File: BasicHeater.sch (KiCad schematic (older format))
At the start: 10 parts, among them J13 Thermistor

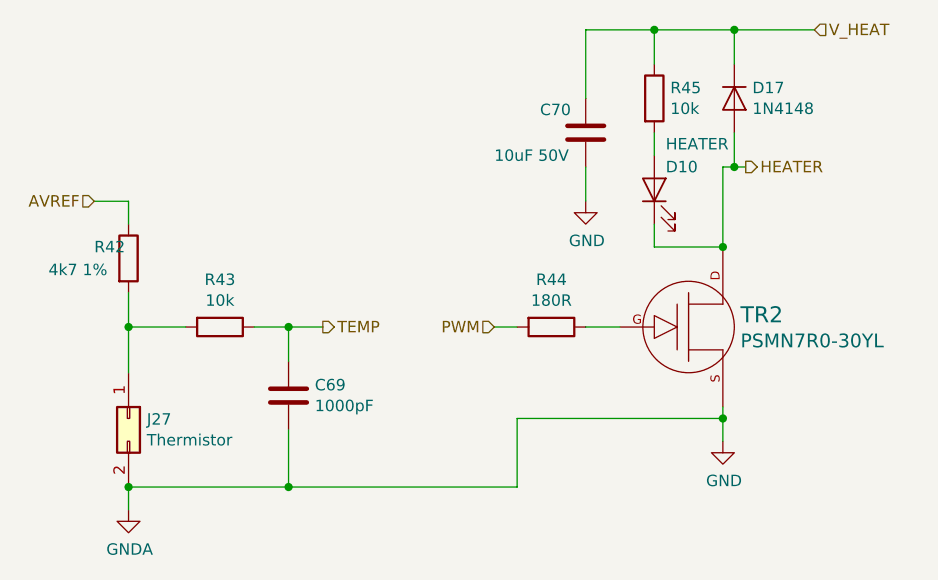
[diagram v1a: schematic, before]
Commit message: Add missing files from the TMC2130 branch.
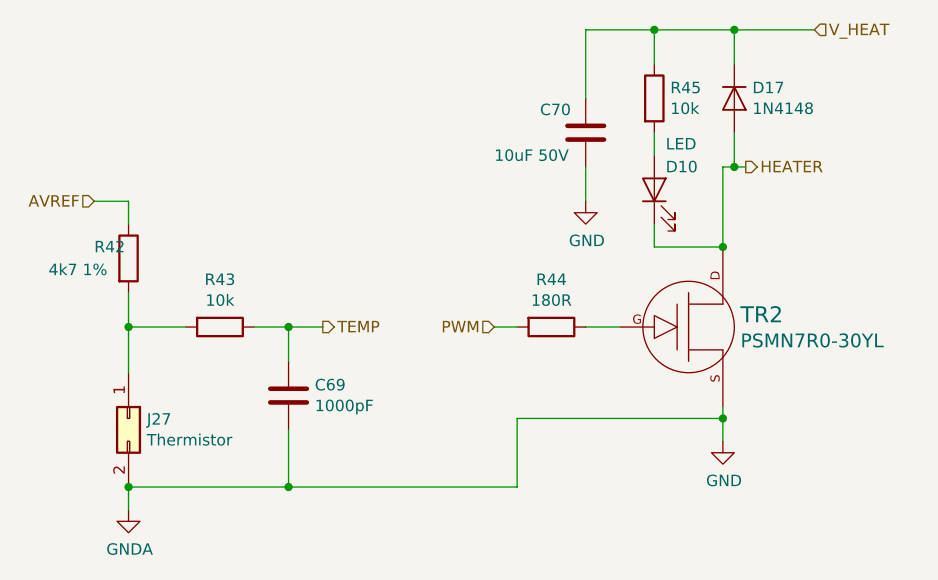
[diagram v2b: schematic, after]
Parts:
- C16: footprint Capacitor_SMD:C_0603_1608Metric -> PrntrBoardV1:C_0603_1608Metric
- C17: footprint Capacitor_SMD:C_1206_3216Metric -> PrntrBoardV1:C_1206_3216Metric
- D2: value HEATER -> LED
- R10, R11, R8, R9: footprint Resistor_SMD:R_0603_1608Metric -> PrntrBoardV1:R_0603_1608Metric
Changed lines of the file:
@@
 F 0 "R42" H 2800 3000 50  0000 L CNN
 F 1 "4k7 1%" H 2600 2900 50  0000 L CNN
-F 2 "Resistor_SMD:R_0603_1608Metric" V 2880 2950 50  0001 C CNN
+F 2 "PrntrBoardV1:R_0603_1608Metric" V 2880 2950 50  0001 C CNN
 F 3 "~" H 2950 2950 50  0001 C CNN
 	1    2950 2950
@@
 F 0 "R43" V 3143 3250 50  0000 C CNN
 F 1 "10k" V 3234 3250 50  0000 C CNN
-F 2 "Resistor_SMD:R_0603_1608Metric" V 3280 3250 50  0001 C CNN
+F 2 "PrntrBoardV1:R_0603_1608Metric" V 3280 3250 50  0001 C CNN
 F 3 "~" H 3350 3250 50  0001 C CNN
 	1    3350 3250
@@
 F 0 "C69" H 3765 3596 50  0000 L CNN
 F 1 "1000pF" H 3765 3505 50  0000 L CNN
-F 2 "Capacitor_SMD:C_0603_1608Metric" H 3688 3400 50  0001 C CNN
+F 2 "PrntrBoardV1:C_0603_1608Metric" H 3688 3400 50  0001 C CNN
 F 3 "~" H 3650 3550 50  0001 C CNN
 	1    3650 3550
@@
 F 0 "R44" V 4593 3250 50  0000 C CNN
 F 1 "180R" V 4684 3250 50  0000 C CNN
-F 2 "Resistor_SMD:R_0603_1608Metric" V 4730 3250 50  0001 C CNN
+F 2 "PrntrBoardV1:R_0603_1608Metric" V 4730 3250 50  0001 C CNN
 F 3 "~" H 4800 3250 50  0001 C CNN
 	1    4800 3250
@@
 F 0 "C70" H 4750 2500 50  0000 L CNN
 F 1 "10uF 50V" H 4550 2300 50  0000 L CNN
-F 2 "Capacitor_SMD:C_1206_3216Metric" H 4950 2400 50  0001 C CNN
+F 2 "PrntrBoardV1:C_1206_3216Metric" H 4950 2400 50  0001 C CNN
 F 3 "~" H 4950 2400 50  0001 C CNN
 	1    4950 2400
@@
 F 0 "R45" H 5320 2296 50  0000 L CNN
 F 1 "10k" H 5320 2205 50  0000 L CNN
-F 2 "Resistor_SMD:R_0603_1608Metric" V 5180 2250 50  0001 C CNN
+F 2 "PrntrBoardV1:R_0603_1608Metric" V 5180 2250 50  0001 C CNN
 F 3 "~" H 5250 2250 50  0001 C CNN
 	1    5250 2250
@@
 AR Path="/5AB8F10D/5ACEEAB5" Ref="D11"  Part="1"
 F 0 "D10" V 5350 2600 50  0000 R CNN
-F 1 "HEATER" V 5450 2600 50  0000 R CNN
+F 1 "LED" V 5450 2600 50  0000 R CNN
 F 2 "PrntrBoardV1:LED_0603_1608Metric" H 5250 2650 50  0001 C CNN
 F 3 "~" H 5250 2650 50  0001 C CNN

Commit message: Reset schematics for tmc2660. Clean the board layout.
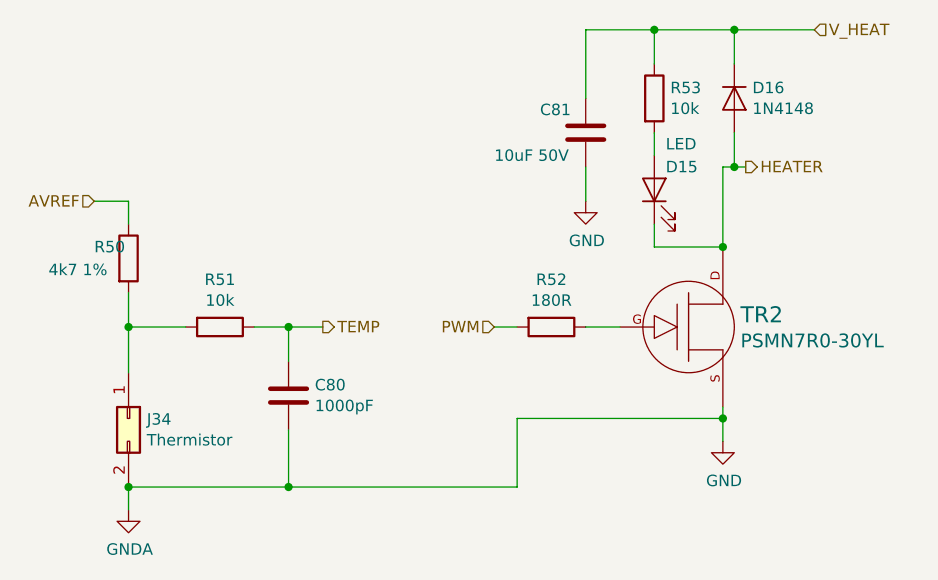
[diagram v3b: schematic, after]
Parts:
- renumbered C16 to C23, C17 to C24, D17 to D16, D2 to D6, J13 to J20, R8 to R16, R9 to R17, R10 to R18, R11 to R19
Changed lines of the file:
@@
 $EndDescr
 $Comp
-L Connector_Generic:Conn_02x01 J13
+L Connector_Generic:Conn_02x01 J20
 U 1 1 5ACEEAAB
 P 2950 3650
-AR Path="/5AC337B6/5ACBE919/5AD4D269/5ACEEAAB" Ref="J13"  Part="1"
-AR Path="/5AC337B6/5AD9F95A/5AD4D269/5ACEEAAB" Ref="J27"  Part="1"
-AR Path="/5AB8F10D/5ACEEAAB" Ref="J28"  Part="1"
-F 0 "J27" V 2954 3730 50  0000 L CNN
+AR Path="/5AC337B6/5ACBE919/5AD4D269/5ACEEAAB" Ref="J20"  Part="1"
+AR Path="/5AC337B6/5AD9F95A/5AD4D269/5ACEEAAB" Ref="J34"  Part="1"
+AR Path="/5AB8F10D/5ACEEAAB" Ref="J?"  Part="1"
+F 0 "J34" V 2954 3730 50  0000 L CNN
 F 1 "Thermistor" V 3045 3730 50  0000 L CNN
 F 2 "Connector_PinHeader_2.54mm:PinHeader_1x02_P2.54mm_Vertical" H 2950 3650 50  0001 C CNN
@@
 $EndComp
 $Comp
-L power:GNDA #PWR020
+L power:GNDA #PWR031
 U 1 1 5ACEEAAC
 P 2950 4050
-AR Path="/5AC337B6/5ACBE919/5AD4D269/5ACEEAAC" Ref="#PWR020"  Part="1"
-AR Path="/5AC337B6/5AD9F95A/5AD4D269/5ACEEAAC" Ref="#PWR065"  Part="1"
-AR Path="/5AB8F10D/5ACEEAAC" Ref="#PWR068"  Part="1"
-F 0 "#PWR065" H 2950 3800 50  0001 C CNN
+AR Path="/5AC337B6/5ACBE919/5AD4D269/5ACEEAAC" Ref="#PWR031"  Part="1"
+AR Path="/5AC337B6/5AD9F95A/5AD4D269/5ACEEAAC" Ref="#PWR076"  Part="1"
+AR Path="/5AB8F10D/5ACEEAAC" Ref="#PWR?"  Part="1"
+F 0 "#PWR076" H 2950 3800 50  0001 C CNN
 F 1 "GNDA" H 2955 3877 50  0000 C CNN
 F 2 "" H 2950 4050 50  0001 C CNN
@@
 $EndComp
 $Comp
-L Device:R R8
+L Device:R R16
 U 1 1 5ACEEAAD
 P 2950 2950
-AR Path="/5AC337B6/5ACBE919/5AD4D269/5ACEEAAD" Ref="R8"  Part="1"
-AR Path="/5AC337B6/5AD9F95A/5AD4D269/5ACEEAAD" Ref="R42"  Part="1"
-AR Path="/5AB8F10D/5ACEEAAD" Ref="R46"  Part="1"
-F 0 "R42" H 2800 3000 50  0000 L CNN
+AR Path="/5AC337B6/5ACBE919/5AD4D269/5ACEEAAD" Ref="R16"  Part="1"
+AR Path="/5AC337B6/5AD9F95A/5AD4D269/5ACEEAAD" Ref="R50"  Part="1"
+AR Path="/5AB8F10D/5ACEEAAD" Ref="R?"  Part="1"
+F 0 "R50" H 2800 3000 50  0000 L CNN
 F 1 "4k7 1%" H 2600 2900 50  0000 L CNN
 F 2 "PrntrBoardV1:R_0603_1608Metric" V 2880 2950 50  0001 C CNN
@@
 $EndComp
 $Comp
-L Device:R R9
+L Device:R R17
 U 1 1 5ACEEAAE
 P 3350 3250
-AR Path="/5AC337B6/5ACBE919/5AD4D269/5ACEEAAE" Ref="R9"  Part="1"
-AR Path="/5AC337B6/5AD9F95A/5AD4D269/5ACEEAAE" Ref="R43"  Part="1"
-AR Path="/5AB8F10D/5ACEEAAE" Ref="R47"  Part="1"
-F 0 "R43" V 3143 3250 50  0000 C CNN
+AR Path="/5AC337B6/5ACBE919/5AD4D269/5ACEEAAE" Ref="R17"  Part="1"
+AR Path="/5AC337B6/5AD9F95A/5AD4D269/5ACEEAAE" Ref="R51"  Part="1"
+AR Path="/5AB8F10D/5ACEEAAE" Ref="R?"  Part="1"
+F 0 "R51" V 3143 3250 50  0000 C CNN
 F 1 "10k" V 3234 3250 50  0000 C CNN
 F 2 "PrntrBoardV1:R_0603_1608Metric" V 3280 3250 50  0001 C CNN
@@
 $EndComp
 $Comp
-L Device:C C16
+L Device:C C23
 U 1 1 5AD4D569
 P 3650 3550
-AR Path="/5AC337B6/5ACBE919/5AD4D269/5AD4D569" Ref="C16"  Part="1"
-AR Path="/5AC337B6/5AD9F95A/5AD4D269/5AD4D569" Ref="C69"  Part="1"
-AR Path="/5AB8F10D/5AD4D569" Ref="C71"  Part="1"
-F 0 "C69" H 3765 3596 50  0000 L CNN
+AR Path="/5AC337B6/5ACBE919/5AD4D269/5AD4D569" Ref="C23"  Part="1"
+AR Path="/5AC337B6/5AD9F95A/5AD4D269/5AD4D569" Ref="C80"  Part="1"
+AR Path="/5AB8F10D/5AD4D569" Ref="C?"  Part="1"
+F 0 "C80" H 3765 3596 50  0000 L CNN
 F 1 "1000pF" H 3765 3505 50  0000 L CNN
 F 2 "PrntrBoardV1:C_0603_1608Metric" H 3688 3400 50  0001 C CNN
@@
 PWM
 $Comp
-L Device:R R10
+L Device:R R18
 U 1 1 5ACEEAB0
 P 4800 3250
-AR Path="/5AC337B6/5ACBE919/5AD4D269/5ACEEAB0" Ref="R10"  Part="1"
-AR Path="/5AC337B6/5AD9F95A/5AD4D269/5ACEEAB0" Ref="R44"  Part="1"
-AR Path="/5AB8F10D/5ACEEAB0" Ref="R48"  Part="1"
-F 0 "R44" V 4593 3250 50  0000 C CNN
+AR Path="/5AC337B6/5ACBE919/5AD4D269/5ACEEAB0" Ref="R18"  Part="1"
+AR Path="/5AC337B6/5AD9F95A/5AD4D269/5ACEEAB0" Ref="R52"  Part="1"
+AR Path="/5AB8F10D/5ACEEAB0" Ref="R?"  Part="1"
+F 0 "R52" V 4593 3250 50  0000 C CNN
 F 1 "180R" V 4684 3250 50  0000 C CNN
 F 2 "PrntrBoardV1:R_0603_1608Metric" V 4730 3250 50  0001 C CNN
@@
 AR Path="/5AC337B6/5ACBE919/5AD4D269/5AD51003" Ref="TR1"  Part="1"
 AR Path="/5AC337B6/5AD9F95A/5AD4D269/5AD51003" Ref="TR2"  Part="1"
-AR Path="/5AB8F10D/5AD51003" Ref="TR3"  Part="1"
+AR Path="/5AB8F10D/5AD51003" Ref="TR?"  Part="1"
 F 0 "TR2" H 5627 3303 70  0000 L CNN
 F 1 "PSMN7R0-30YL" H 5627 3189 60  0000 L CNN
@@
 	4950 3250 5100 3250
 $Comp
-L power:GND #PWR022
+L power:GND #PWR033
 U 1 1 5AD51105
 P 5550 3750
-AR Path="/5AC337B6/5ACBE919/5AD4D269/5AD51105" Ref="#PWR022"  Part="1"
-AR Path="/5AC337B6/5AD9F95A/5AD4D269/5AD51105" Ref="#PWR067"  Part="1"
-AR Path="/5AB8F10D/5AD51105" Ref="#PWR070"  Part="1"
-F 0 "#PWR067" H 5550 3500 50  0001 C CNN
+AR Path="/5AC337B6/5ACBE919/5AD4D269/5AD51105" Ref="#PWR033"  Part="1"
+AR Path="/5AC337B6/5AD9F95A/5AD4D269/5AD51105" Ref="#PWR078"  Part="1"
+AR Path="/5AB8F10D/5AD51105" Ref="#PWR?"  Part="1"
+F 0 "#PWR078" H 5550 3500 50  0001 C CNN
 F 1 "GND" H 5555 3577 50  0000 C CNN
 F 2 "" H 5550 3750 50  0001 C CNN
@@
 	5550 3600 5550 3650
 $Comp
-L Device:C C17
+L Device:C C24
 U 1 1 5AD51206
 P 4950 2400
-AR Path="/5AC337B6/5ACBE919/5AD4D269/5AD51206" Ref="C17"  Part="1"
-AR Path="/5AC337B6/5AD9F95A/5AD4D269/5AD51206" Ref="C70"  Part="1"
-AR Path="/5AB8F10D/5AD51206" Ref="C72"  Part="1"
-F 0 "C70" H 4750 2500 50  0000 L CNN
+AR Path="/5AC337B6/5ACBE919/5AD4D269/5AD51206" Ref="C24"  Part="1"
+AR Path="/5AC337B6/5AD9F95A/5AD4D269/5AD51206" Ref="C81"  Part="1"
+AR Path="/5AB8F10D/5AD51206" Ref="C?"  Part="1"
+F 0 "C81" H 4750 2500 50  0000 L CNN
 F 1 "10uF 50V" H 4550 2300 50  0000 L CNN
 F 2 "PrntrBoardV1:C_1206_3216Metric" H 4950 2400 50  0001 C CNN
@@
 $EndComp
 $Comp
-L Device:R R11
+L Device:R R19
 U 1 1 5AD512CE
 P 5250 2250
-AR Path="/5AC337B6/5ACBE919/5AD4D269/5AD512CE" Ref="R11"  Part="1"
-AR Path="/5AC337B6/5AD9F95A/5AD4D269/5AD512CE" Ref="R45"  Part="1"
-AR Path="/5AB8F10D/5AD512CE" Ref="R49"  Part="1"
-F 0 "R45" H 5320 2296 50  0000 L CNN
+AR Path="/5AC337B6/5ACBE919/5AD4D269/5AD512CE" Ref="R19"  Part="1"
+AR Path="/5AC337B6/5AD9F95A/5AD4D269/5AD512CE" Ref="R53"  Part="1"
+AR Path="/5AB8F10D/5AD512CE" Ref="R?"  Part="1"
+F 0 "R53" H 5320 2296 50  0000 L CNN
 F 1 "10k" H 5320 2205 50  0000 L CNN
 F 2 "PrntrBoardV1:R_0603_1608Metric" V 5180 2250 50  0001 C CNN
@@
 $EndComp
 $Comp
-L Device:LED D2
+L Device:LED D6
 U 1 1 5ACEEAB5
 P 5250 2650
-AR Path="/5AC337B6/5ACBE919/5AD4D269/5ACEEAB5" Ref="D2"  Part="1"
-AR Path="/5AC337B6/5AD9F95A/5AD4D269/5ACEEAB5" Ref="D10"  Part="1"
-AR Path="/5AB8F10D/5ACEEAB5" Ref="D11"  Part="1"
-F 0 "D10" V 5350 2600 50  0000 R CNN
+AR Path="/5AC337B6/5ACBE919/5AD4D269/5ACEEAB5" Ref="D6"  Part="1"
+AR Path="/5AC337B6/5AD9F95A/5AD4D269/5ACEEAB5" Ref="D15"  Part="1"
+AR Path="/5AB8F10D/5ACEEAB5" Ref="D?"  Part="1"
+F 0 "D15" V 5350 2600 50  0000 R CNN
 F 1 "LED" V 5450 2600 50  0000 R CNN
 F 2 "PrntrBoardV1:LED_0603_1608Metric" H 5250 2650 50  0001 C CNN
@@
 $EndComp
 $Comp
-L power:GND #PWR021
+L power:GND #PWR032
 U 1 1 5ACEEAB6
 P 4950 2700
-AR Path="/5AC337B6/5ACBE919/5AD4D269/5ACEEAB6" Ref="#PWR021"  Part="1"
-AR Path="/5AC337B6/5AD9F95A/5AD4D269/5ACEEAB6" Ref="#PWR066"  Part="1"
-AR Path="/5AB8F10D/5ACEEAB6" Ref="#PWR069"  Part="1"
-F 0 "#PWR066" H 4950 2450 50  0001 C CNN
+AR Path="/5AC337B6/5ACBE919/5AD4D269/5ACEEAB6" Ref="#PWR032"  Part="1"
+AR Path="/5AC337B6/5AD9F95A/5AD4D269/5ACEEAB6" Ref="#PWR077"  Part="1"
+AR Path="/5AB8F10D/5ACEEAB6" Ref="#PWR?"  Part="1"
+F 0 "#PWR077" H 4950 2450 50  0001 C CNN
 F 1 "GND" H 4955 2527 50  0000 C CNN
 F 2 "" H 4950 2700 50  0001 C CNN
@@
 	5550 3650 5550 3750
 $Comp
-L Device:D D17
+L Device:D D16
 U 1 1 5ACF27DC
 P 5600 2250
-AR Path="/5AC337B6/5AD9F95A/5AD4D269/5ACF27DC" Ref="D17"  Part="1"
-AR Path="/5AC337B6/5ACBE919/5AD4D269/5ACF27DC" Ref="D16"  Part="1"
-F 0 "D17" V 5554 2329 50  0000 L CNN
+AR Path="/5AC337B6/5AD9F95A/5AD4D269/5ACF27DC" Ref="D16"  Part="1"
+AR Path="/5AC337B6/5ACBE919/5AD4D269/5ACF27DC" Ref="D7"  Part="1"
+F 0 "D16" V 5554 2329 50  0000 L CNN
 F 1 "1N4148" V 5645 2329 50  0000 L CNN
 F 2 "Diode_SMD:D_SOD-323_HandSoldering" H 5600 2250 50  0001 C CNN

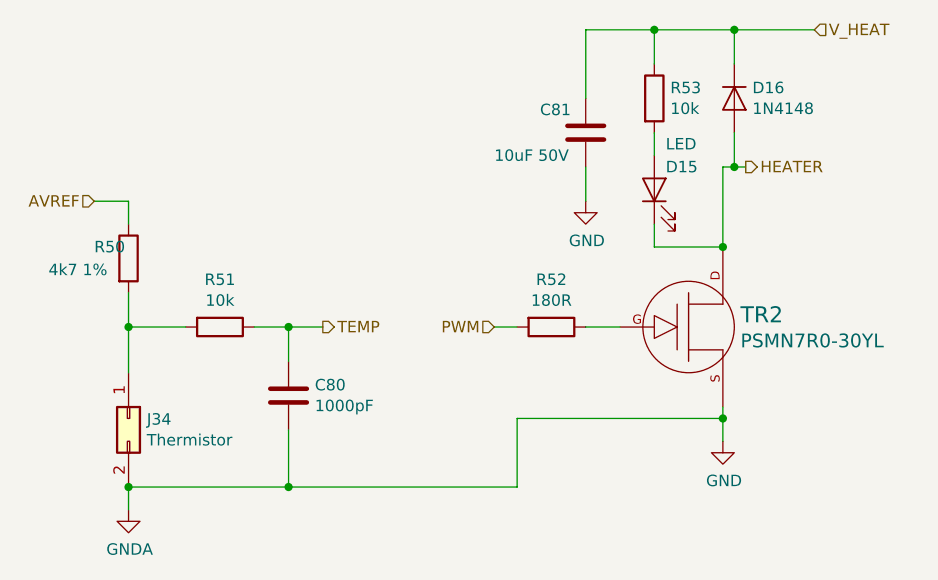
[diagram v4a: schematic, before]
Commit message: Updated motor connectors to Molex SL style.
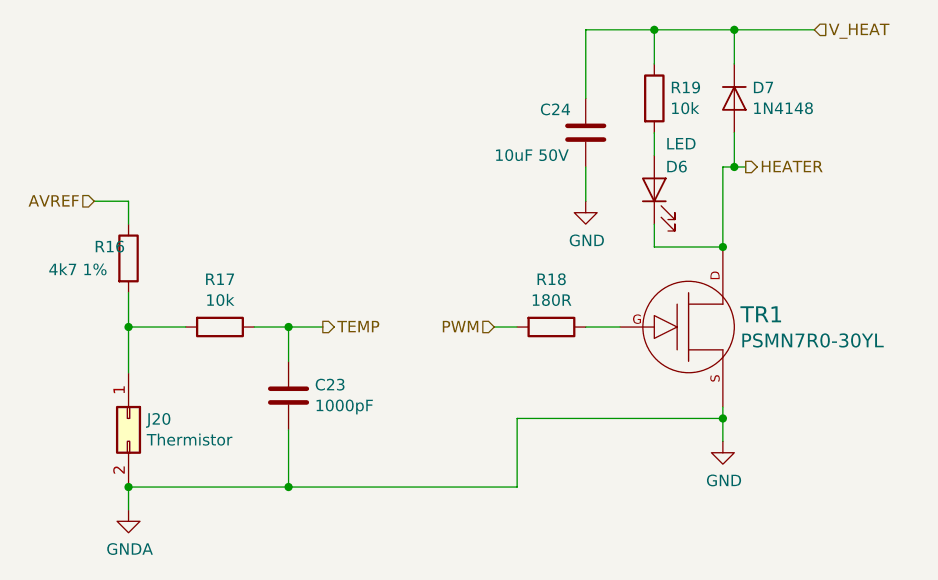
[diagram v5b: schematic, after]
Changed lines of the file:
@@
 $Descr A4 11693 8268
 encoding utf-8
-Sheet 29 35
+Sheet 7 35
 Title ""
 Date ""
@@
 AR Path="/5AC337B6/5AD9F95A/5AD4D269/5ACEEAAB" Ref="J34"  Part="1"
 AR Path="/5AB8F10D/5ACEEAAB" Ref="J?"  Part="1"
-F 0 "J34" V 2954 3730 50  0000 L CNN
+F 0 "J20" V 2954 3730 50  0000 L CNN
 F 1 "Thermistor" V 3045 3730 50  0000 L CNN
 F 2 "Connector_PinHeader_2.54mm:PinHeader_1x02_P2.54mm_Vertical" H 2950 3650 50  0001 C CNN
@@
 AR Path="/5AC337B6/5AD9F95A/5AD4D269/5ACEEAAC" Ref="#PWR076"  Part="1"
 AR Path="/5AB8F10D/5ACEEAAC" Ref="#PWR?"  Part="1"
-F 0 "#PWR076" H 2950 3800 50  0001 C CNN
+F 0 "#PWR031" H 2950 3800 50  0001 C CNN
 F 1 "GNDA" H 2955 3877 50  0000 C CNN
 F 2 "" H 2950 4050 50  0001 C CNN
@@
 AR Path="/5AC337B6/5AD9F95A/5AD4D269/5ACEEAAD" Ref="R50"  Part="1"
 AR Path="/5AB8F10D/5ACEEAAD" Ref="R?"  Part="1"
-F 0 "R50" H 2800 3000 50  0000 L CNN
+F 0 "R16" H 2800 3000 50  0000 L CNN
 F 1 "4k7 1%" H 2600 2900 50  0000 L CNN
 F 2 "PrntrBoardV1:R_0603_1608Metric" V 2880 2950 50  0001 C CNN
@@
 AR Path="/5AC337B6/5AD9F95A/5AD4D269/5ACEEAAE" Ref="R51"  Part="1"
 AR Path="/5AB8F10D/5ACEEAAE" Ref="R?"  Part="1"
-F 0 "R51" V 3143 3250 50  0000 C CNN
+F 0 "R17" V 3143 3250 50  0000 C CNN
 F 1 "10k" V 3234 3250 50  0000 C CNN
 F 2 "PrntrBoardV1:R_0603_1608Metric" V 3280 3250 50  0001 C CNN
@@
 AR Path="/5AC337B6/5AD9F95A/5AD4D269/5AD4D569" Ref="C80"  Part="1"
 AR Path="/5AB8F10D/5AD4D569" Ref="C?"  Part="1"
-F 0 "C80" H 3765 3596 50  0000 L CNN
+F 0 "C23" H 3765 3596 50  0000 L CNN
 F 1 "1000pF" H 3765 3505 50  0000 L CNN
 F 2 "PrntrBoardV1:C_0603_1608Metric" H 3688 3400 50  0001 C CNN
@@
 AR Path="/5AC337B6/5AD9F95A/5AD4D269/5ACEEAB0" Ref="R52"  Part="1"
 AR Path="/5AB8F10D/5ACEEAB0" Ref="R?"  Part="1"
-F 0 "R52" V 4593 3250 50  0000 C CNN
+F 0 "R18" V 4593 3250 50  0000 C CNN
 F 1 "180R" V 4684 3250 50  0000 C CNN
 F 2 "PrntrBoardV1:R_0603_1608Metric" V 4730 3250 50  0001 C CNN
@@
 AR Path="/5AC337B6/5AD9F95A/5AD4D269/5AD51003" Ref="TR2"  Part="1"
 AR Path="/5AB8F10D/5AD51003" Ref="TR?"  Part="1"
-F 0 "TR2" H 5627 3303 70  0000 L CNN
+F 0 "TR1" H 5627 3303 70  0000 L CNN
 F 1 "PSMN7R0-30YL" H 5627 3189 60  0000 L CNN
 F 2 "PrntrBoardV1:SOT-669_LFPAK" H 5400 3250 60  0001 C CNN
@@
 AR Path="/5AC337B6/5AD9F95A/5AD4D269/5AD51105" Ref="#PWR078"  Part="1"
 AR Path="/5AB8F10D/5AD51105" Ref="#PWR?"  Part="1"
-F 0 "#PWR078" H 5550 3500 50  0001 C CNN
+F 0 "#PWR033" H 5550 3500 50  0001 C CNN
 F 1 "GND" H 5555 3577 50  0000 C CNN
 F 2 "" H 5550 3750 50  0001 C CNN
@@
 AR Path="/5AC337B6/5AD9F95A/5AD4D269/5AD51206" Ref="C81"  Part="1"
 AR Path="/5AB8F10D/5AD51206" Ref="C?"  Part="1"
-F 0 "C81" H 4750 2500 50  0000 L CNN
+F 0 "C24" H 4750 2500 50  0000 L CNN
 F 1 "10uF 50V" H 4550 2300 50  0000 L CNN
 F 2 "PrntrBoardV1:C_1206_3216Metric" H 4950 2400 50  0001 C CNN
@@
 AR Path="/5AC337B6/5AD9F95A/5AD4D269/5AD512CE" Ref="R53"  Part="1"
 AR Path="/5AB8F10D/5AD512CE" Ref="R?"  Part="1"
-F 0 "R53" H 5320 2296 50  0000 L CNN
+F 0 "R19" H 5320 2296 50  0000 L CNN
 F 1 "10k" H 5320 2205 50  0000 L CNN
 F 2 "PrntrBoardV1:R_0603_1608Metric" V 5180 2250 50  0001 C CNN
@@
 AR Path="/5AC337B6/5AD9F95A/5AD4D269/5ACEEAB5" Ref="D15"  Part="1"
 AR Path="/5AB8F10D/5ACEEAB5" Ref="D?"  Part="1"
-F 0 "D15" V 5350 2600 50  0000 R CNN
+F 0 "D6" V 5350 2600 50  0000 R CNN
 F 1 "LED" V 5450 2600 50  0000 R CNN
 F 2 "PrntrBoardV1:LED_0603_1608Metric" H 5250 2650 50  0001 C CNN
@@
 AR Path="/5AC337B6/5AD9F95A/5AD4D269/5ACEEAB6" Ref="#PWR077"  Part="1"
 AR Path="/5AB8F10D/5ACEEAB6" Ref="#PWR?"  Part="1"
-F 0 "#PWR077" H 4950 2450 50  0001 C CNN
+F 0 "#PWR032" H 4950 2450 50  0001 C CNN
 F 1 "GND" H 4955 2527 50  0000 C CNN
 F 2 "" H 4950 2700 50  0001 C CNN
@@
 AR Path="/5AC337B6/5AD9F95A/5AD4D269/5ACF27DC" Ref="D16"  Part="1"
 AR Path="/5AC337B6/5ACBE919/5AD4D269/5ACF27DC" Ref="D7"  Part="1"
-F 0 "D16" V 5554 2329 50  0000 L CNN
+F 0 "D7" V 5554 2329 50  0000 L CNN
 F 1 "1N4148" V 5645 2329 50  0000 L CNN
 F 2 "Diode_SMD:D_SOD-323_HandSoldering" H 5600 2250 50  0001 C CNN
